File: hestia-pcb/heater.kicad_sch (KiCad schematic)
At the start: 22 parts, among them Q1 FDS8876, SW2 SW_Push_Open, U10 INA826

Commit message: shift template designator/value locations for SRP5030C footprint in library. Update hestia PCB with SRP5030C footprint for L2 on buck regulator. change D7 footprint from SOT23 to smaller SOT-323 as per diode on BOM.
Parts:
- D7: footprint Package_TO_SOT_SMD:SOT-23 -> Package_TO_SOT_SMD:SOT-323_SC-70_Handsoldering
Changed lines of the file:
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@@
       (effects (font (size 1.27 1.27)) (justify left))
     )
-    (property "Footprint" "Package_TO_SOT_SMD:SOT-23" (at 59.055 49.53 0)
+    (property "Footprint" "Package_TO_SOT_SMD:SOT-323_SC-70_Handsoldering" (at 59.055 49.53 0)
       (effects (font (size 1.27 1.27)) (justify left) hide)
     )

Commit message: #28: bump version to 2.1
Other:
- company: (none) -> Mawson Rovers
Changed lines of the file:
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@@
 (kicad_sch (version 20230121) (generator eeschema)
   (paper "A4")
+  (title_block
+    (company "Mawson Rovers")
+  )
   (junction (at 103.505 56.515) (diameter 0) (color 0 0 0 0)
   )

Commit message: added new themal switch footprint to hestia lib. Added 3 wire restraint hole footprints -> 1.2mm, 1.8mm and 1.9mm. Change adc wire restraint holes (H9 to H13) to 1.8mm. Change uC wire restraint holes(H14 & H15) to 1.8mm & moved H14 & H15 designators. Change thermal switch wire restraint holes (H16 & H17) to 1.9mm & also shifted hole coords left 0.2mm & moved H16 & H17 designators. Change thermal switch footprint to new footprint with thruhole pads to 1.2mm dia hole as well as with increased pad distance. Thicken VCC traces to thermal switch - have to revisit to satisfy DRC - probably change multiple traces to signal polygon. Added two GND vias for extra GND stitching off J2. ToDo -Resolve DRC issues. Some padd may need extra signal spurs to pads - just manually adding a trace to the pads may satisfy the DRC requirement
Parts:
- SW2: footprint Connector_PinHeader_2.54mm:PinHeader_1x02_P2.54mm_Vertical -> Hestia:Thermal Switch
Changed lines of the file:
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@@
       (effects (font (size 1.27 1.27)) (justify right))
     )
-    (property "Footprint" "Connector_PinHeader_2.54mm:PinHeader_1x02_P2.54mm_Vertical" (at 124.46 78.74 0)
+    (property "Footprint" "Hestia:Thermal Switch" (at 124.46 78.74 0)
       (effects (font (size 1.27 1.27)) hide)
     )

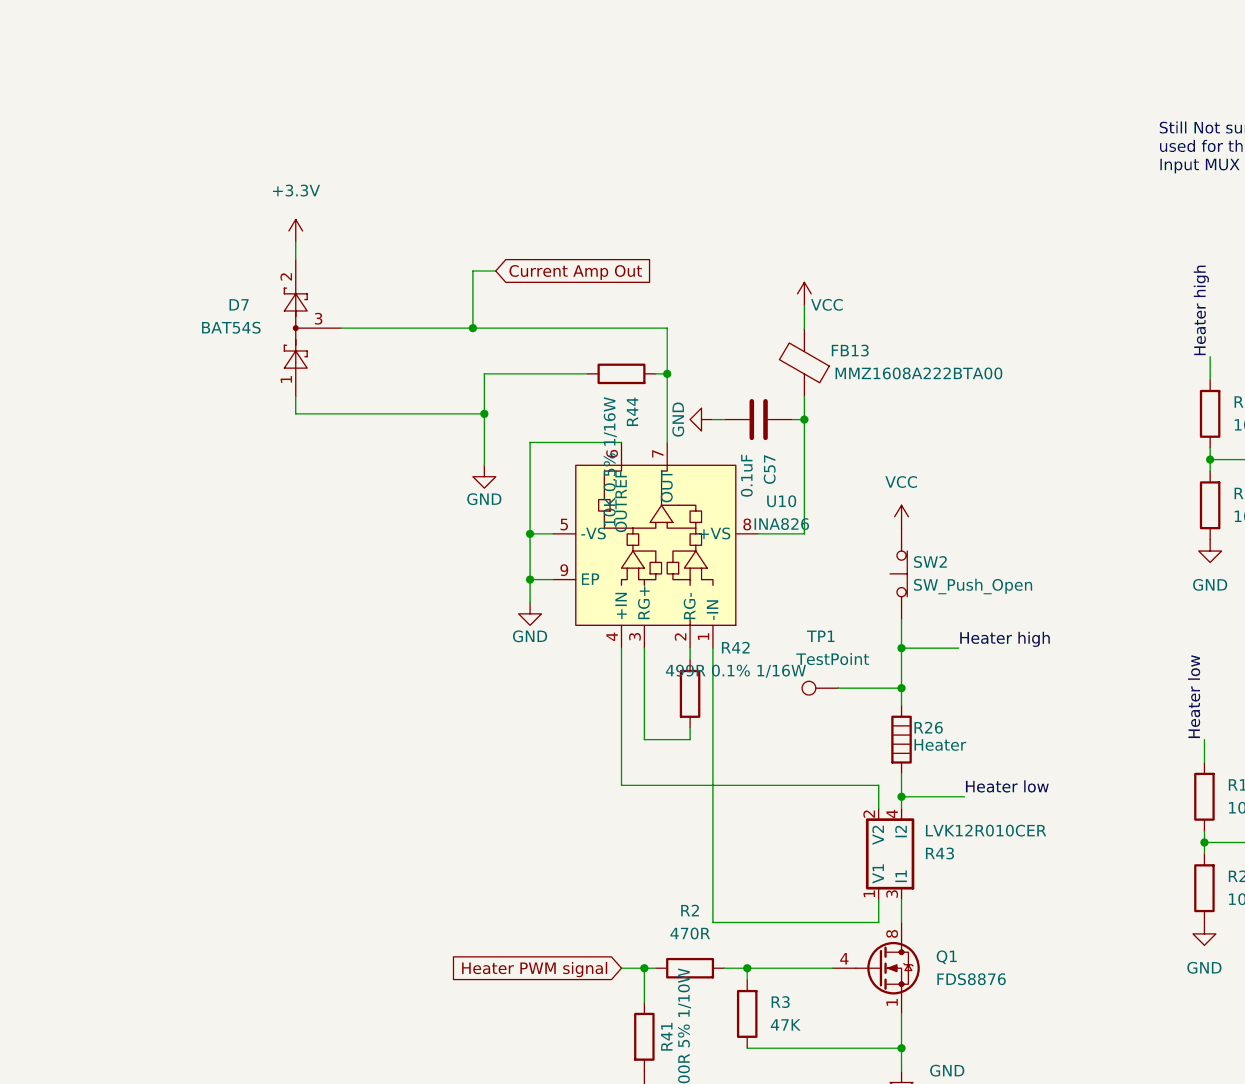
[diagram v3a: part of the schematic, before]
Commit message: #35: add TP7 low side heater test point to schematic
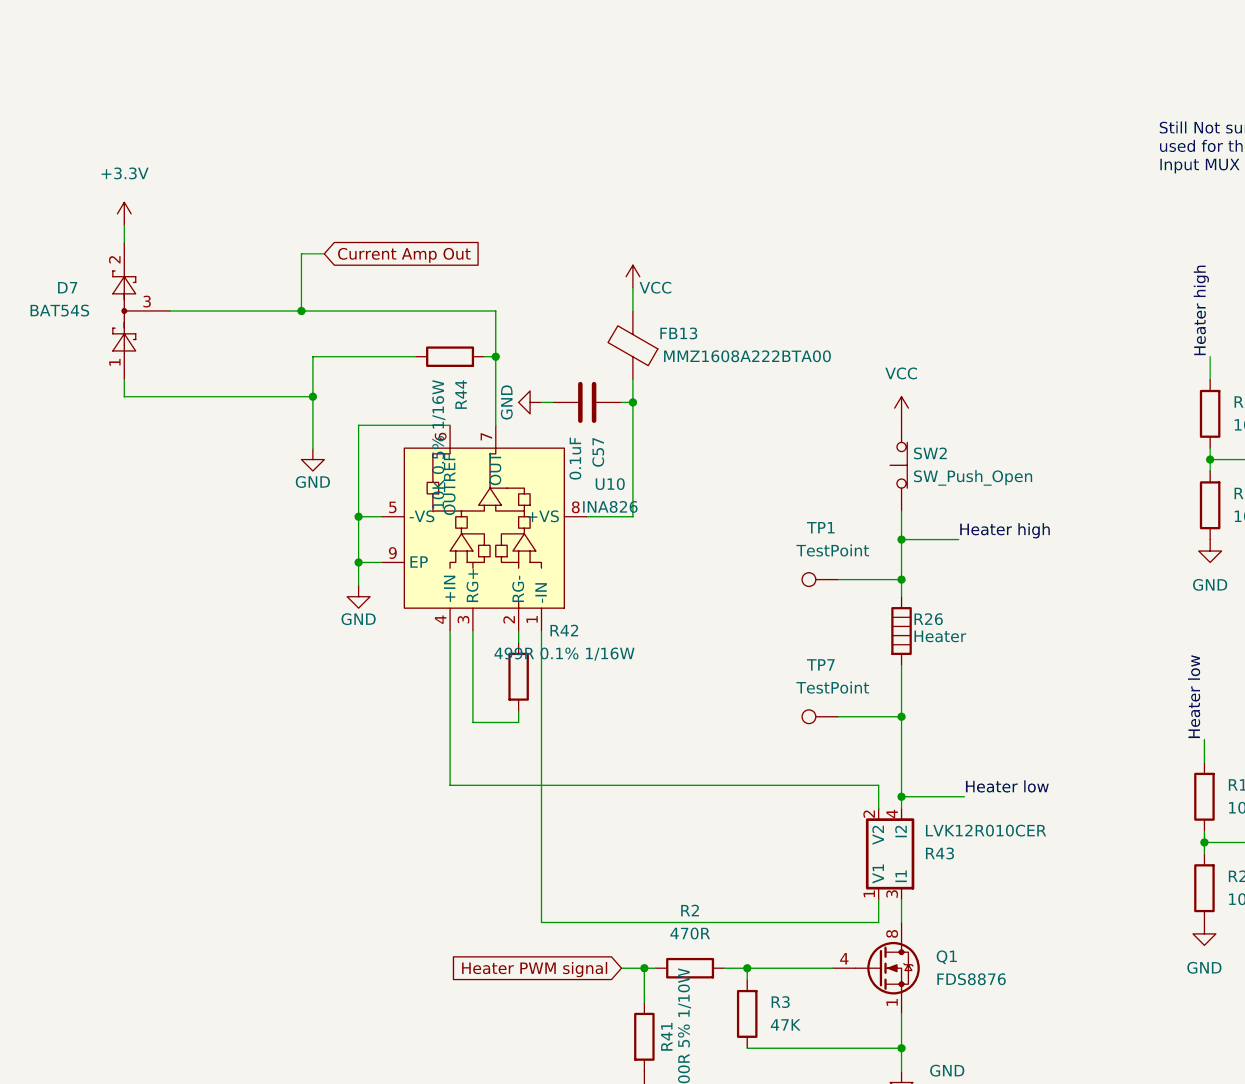
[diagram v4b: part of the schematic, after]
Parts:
- added TP7: TestPoint, TestPoint:TestPoint_Pad_1.0x1.0mm, symbol Connector:TestPoint
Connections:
- net Heater low: now also TP7.1
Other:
- moved on the sheet: C57, D7, FB13, R26, R42, R44, SW2, TP1, U10

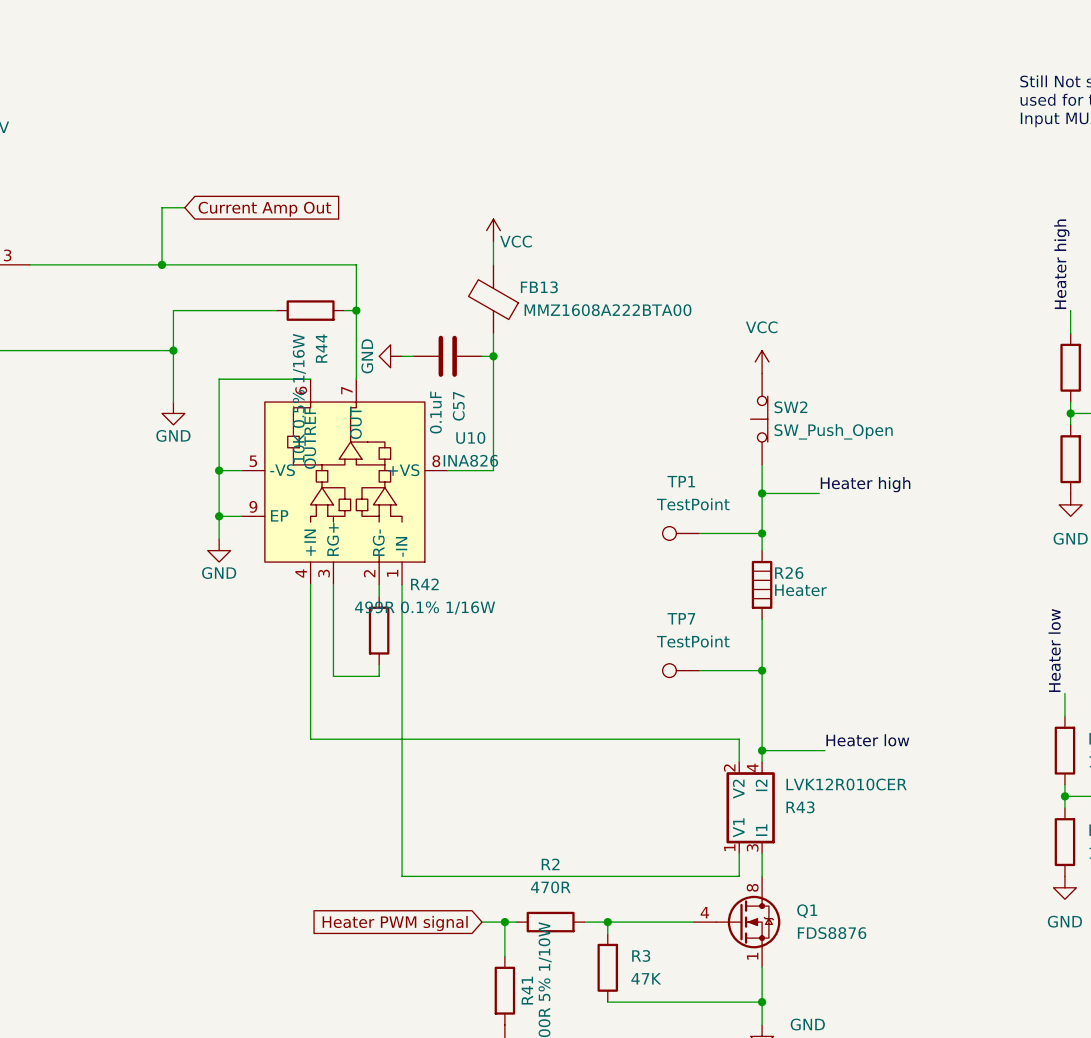
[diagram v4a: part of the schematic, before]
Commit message: reroute current amp out with option resistor to current amp in to directly measure voltage on that side of the current sense resistor. Via added to assist that signal route. add series resistor to current sense line towards uC for current limiting in the case that the low side of the current limiting resistor is experiencing 5V.
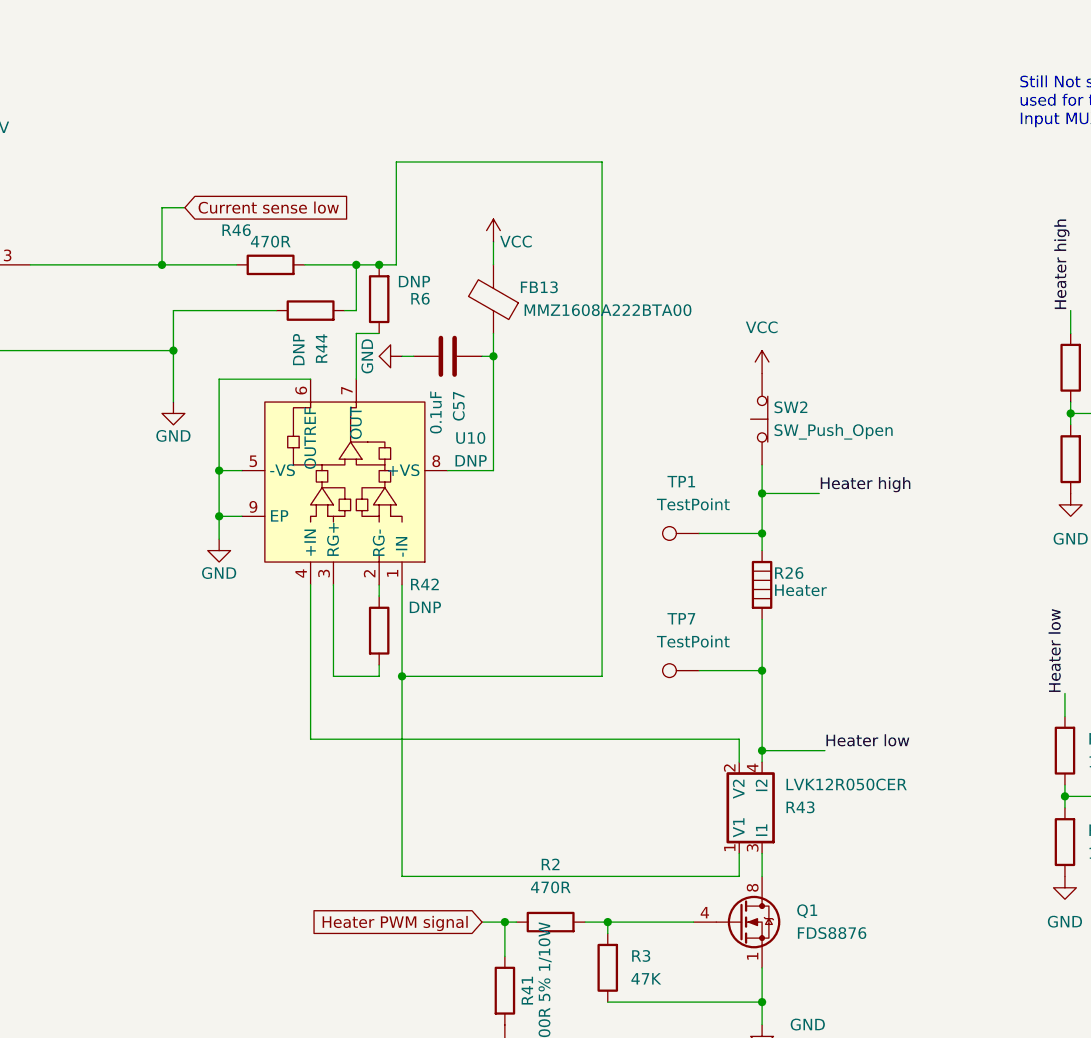
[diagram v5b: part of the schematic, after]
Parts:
- added R46: 470R, Resistor_SMD:R_0603_1608Metric_Pad0.98x0.95mm_HandSolder, symbol Device:R
- added R6: DNP, Resistor_SMD:R_0402_1005Metric_Pad0.72x0.64mm_HandSolder, symbol Device:R
- R42: value 499R 0.1% 1/16W -> DNP
- R43: value LVK12R010CER -> LVK12R050CER; Digikey Part 273-LVK12R010CERCT-ND -> 273-LVK12R050CERCT-ND
- R44: value 10K 0.5% 1/16W -> DNP
- U10: value INA826 -> DNP
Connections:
- net at R43.1 (V1), U10.1 (-IN): now also R44.2, R46.2, R6.2
- removed net Current Amp Out: D7.3, R44.2, U10.7 (OUT)
- new net: R6.1, U10.7 (OUT)
- new net Current sense low: D7.3, R46.1
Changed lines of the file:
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@@
     (company "Mawson Rovers")
   )
-  (junction (at 84.455 54.61) (diameter 0) (color 0 0 0 0)
-  )
   (junction (at 129.54 79.375) (diameter 0) (color 0 0 0 0)
   )
@@
   (junction (at 129.54 94.615) (diameter 0) (color 0 0 0 0)
   )
+  (junction (at 89.535 95.25) (diameter 0) (color 0 0 0 0)
+  )
   (junction (at 64.135 59.055) (diameter 0) (color 0 0 0 0)
   )
+  (junction (at 86.995 49.53) (diameter 0) (color 0 0 0 0)
+  )
   (junction (at 217.805 72.39) (diameter 0) (color 0 0 0 0)
   )
+  (junction (at 84.455 49.53) (diameter 0) (color 0 0 0 0)
+  )
   (junction (at 129.54 131.445) (diameter 0) (color 0 0 0 0)
   )
@@
     (stroke (width 0) (type default))
   )
-  (wire (pts (xy 62.865 49.53) (xy 84.455 49.53))
+  (wire (pts (xy 62.865 49.53) (xy 71.12 49.53))
     (stroke (width 0) (type default))
   )
@@
     (stroke (width 0) (type default))
   )
-  (wire (pts (xy 89.535 85.09) (xy 89.535 117.475))
+  (wire (pts (xy 89.535 85.09) (xy 89.535 95.25))
     (stroke (width 0) (type default))
   )
@@
     (stroke (width 0) (type default))
   )
+  (wire (pts (xy 111.76 95.25) (xy 111.76 38.1))
+    (stroke (width 0) (type default))
+  )
   (wire (pts (xy 129.54 74.93) (xy 135.89 74.93))
     (stroke (width 0) (type default))
@@
     (stroke (width 0) (type default))
   )
-  (wire (pts (xy 84.455 62.23) (xy 84.455 54.61))
-    (stroke (width 0) (type default))
-  )
   (wire (pts (xy 129.54 127.635) (xy 129.54 131.445))
     (stroke (width 0) (type default))
@@
     (stroke (width 0) (type default))
   )
+  (wire (pts (xy 89.535 95.25) (xy 89.535 117.475))
+    (stroke (width 0) (type default))
+  )
   (wire (pts (xy 69.215 72.39) (xy 69.215 77.47))
     (stroke (width 0) (type default))
   )
+  (wire (pts (xy 84.455 57.15) (xy 84.455 62.23))
+    (stroke (width 0) (type default))
+  )
+  (wire (pts (xy 84.455 57.15) (xy 86.995 57.15))
+    (stroke (width 0) (type default))
+  )
   (wire (pts (xy 122.555 94.615) (xy 129.54 94.615))
     (stroke (width 0) (type default))
@@
     (stroke (width 0) (type default))
   )
+  (wire (pts (xy 111.76 38.1) (xy 88.9 38.1))
+    (stroke (width 0) (type default))
+  )
   (wire (pts (xy 129.54 74.93) (xy 129.54 79.375))
     (stroke (width 0) (type default))
@@
     (stroke (width 0) (type default))
   )
+  (wire (pts (xy 89.535 95.25) (xy 111.76 95.25))
+    (stroke (width 0) (type default))
+  )
+  (wire (pts (xy 78.74 49.53) (xy 84.455 49.53))
+    (stroke (width 0) (type default))
+  )
+  (wire (pts (xy 88.9 38.1) (xy 88.9 49.53))
+    (stroke (width 0) (type default))
+  )
   (wire (pts (xy 64.135 59.055) (xy 64.135 64.77))
     (stroke (width 0) (type default))
@@
     (stroke (width 0) (type default))
   )
+  (wire (pts (xy 88.9 49.53) (xy 86.995 49.53))
+    (stroke (width 0) (type default))
+  )
   (wire (pts (xy 129.54 79.375) (xy 129.54 81.28))
     (stroke (width 0) (type default))
@@
   )
   (wire (pts (xy 99.695 57.15) (xy 99.695 59.69))
+    (stroke (width 0) (type default))
+  )
+  (wire (pts (xy 86.995 49.53) (xy 84.455 49.53))
     (stroke (width 0) (type default))
   )
@@
     )
   )
-  (global_label "Current Amp Out" (shape input) (at 65.405 43.18 0) (fields_autoplaced)
+  (global_label "Current sense low" (shape input) (at 65.405 43.18 0) (fields_autoplaced)
     (effects (font (size 1.27 1.27)) (justify left))
-    (property "Intersheetrefs" "${INTERSHEET_REFS}" (at 83.8443 43.1006 0)
+    (property "Intersheetrefs" "${INTERSHEET_REFS}" (at 85.7278 43.18 0)
       (effects (font (size 1.27 1.27)) (justify left) hide)
     )
@@
       (effects (font (size 1.27 1.27)))
     )
-    (property "Value" "INA826" (at 97.155 71.3486 90)
+    (property "Value" "DNP" (at 97.155 71.3486 90)
       (effects (font (size 1.27 1.27)))
     )
@@
     )
   )
+  (symbol (lib_id "Device:R") (at 86.995 53.34 180) (unit 1)
+    (in_bom yes) (on_board yes) (dnp no)
+    (property "Reference" "R6" (at 92.71 53.34 0)
+      (effects (font (size 1.27 1.27)) (justify left))
+    )
+    (property "Value" "DNP" (at 92.71 51.435 0)
+      (effects (font (size 1.27 1.27)) (justify left))
+    )
+    (property "Footprint" "Resistor_SMD:R_0402_1005Metric_Pad0.72x0.64mm_HandSolder" (at 88.773 53.34 90)
+      (effects (font (size 1.27 1.27)) hide)
+    )
+    (property "Datasheet" "~" (at 86.995 53.34 0)
+      (effects (font (size 1.27 1.27)) hide)
+    )
+    (property "Digikey Part" "RMCF0603ZT0R00CT-ND" (at 86.995 53.34 0)
+      (effects (font (size 1.27 1.27)) hide)
+    )
+    (property "Manufacturer" "Stackpole Electronics Inc" (at 86.995 53.34 0)
+      (effects (font (size 1.27 1.27)) hide)
+    )
+    (property "Mfr PN" "RMCF0603ZT0R00" (at 86.995 53.34 0)
+      (effects (font (size 1.27 1.27)) hide)
+    )
+    (property "Type" "SMD" (at 86.995 53.34 0)
+      (effects (font (size 1.27 1.27)) hide)
+    )
+    (pin "1")
+    (pin "2")
+    (instances
+      (project "hestia"
+        (path "/e63e39d7-6ac0-4ffd-8aa3-1841a4541b55"
+          (reference "R6") (unit 1)
+        )
+        (path "/e63e39d7-6ac0-4ffd-8aa3-1841a4541b55/20d49a9a-db00-4709-a347-46ba1cabd595"
+          (reference "R27") (unit 1)
+        )
+      )
+    )
+  )
   (symbol (lib_id "Device:R") (at 106.045 122.555 90) (unit 1)
     (in_bom yes) (on_board yes) (dnp no) (fields_autoplaced)
@@
       (effects (font (size 1.27 1.27)))
     )
-    (property "Value" "499R 0.1% 1/16W" (at 92.075 87.63 0)
+    (property "Value" "DNP" (at 92.075 87.63 0)
       (effects (font (size 1.27 1.27)))
     )
@@
       (effects (font (size 1.27 1.27)) (justify right))
     )
-    (property "Value" "10K 0.5% 1/16W" (at 78.1051 57.15 0)
+    (property "Value" "DNP" (at 78.1051 57.15 0)
       (effects (font (size 1.27 1.27)) (justify right))
     )
@@
       (effects (font (size 1.27 1.27)) (justify right))
     )
-    (property "Value" "LVK12R010CER" (at 132.08 107.315 0)
+    (property "Value" "LVK12R050CER" (at 132.08 107.315 0)
       (effects (font (size 1.27 1.27)) (justify right))
     )
@@
       (effects (font (size 1.27 1.27)) hide)
     )
-    (property "Digikey Part" "273-LVK12R010CERCT-ND" (at 129.54 109.855 0)
+    (property "Digikey Part" "273-LVK12R050CERCT-ND" (at 129.54 109.855 0)
       (effects (font (size 1.27 1.27)) hide)
     )
@@
         )
       )
+    )
+  )
+  (symbol (lib_id "Device:R") (at 74.93 49.53 90) (unit 1)
+    (in_bom yes) (on_board yes) (dnp no)
+    (property "Reference" "R46" (at 71.12 45.72 90)
+      (effects (font (size 1.27 1.27)))
+    )
+    (property "Value" "470R" (at 74.93 46.99 90)
+      (effects (font (size 1.27 1.27)))
+    )
+    (property "Footprint" "Resistor_SMD:R_0603_1608Metric_Pad0.98x0.95mm_HandSolder" (at 74.93 51.308 90)
+      (effects (font (size 1.27 1.27)) hide)
+    )
+    (property "Datasheet" "~" (at 74.93 49.53 0)
+      (effects (font (size 1.27 1.27)) hide)
+    )
+    (property "Digikey Part" "RHM470ADCT-ND" (at 74.93 49.53 90)
+      (effects (font (size 1.27 1.27)) hide)
+    )
+    (property "Manufacturer" "Rohm Semiconductor" (at 74.93 49.53 0)
+      (effects (font (size 1.27 1.27)) hide)
+    )
+    (property "Mfr PN" "ESR03EZPF4700" (at 74.93 49.53 0)
+      (effects (font (size 1.27 1.27)) hide)
+    )
+    (property "Type" "SMD" (at 74.93 49.53 0)
+      (effects (font (size 1.27 1.27)) hide)
+    )
+    (pin "1")
+    (pin "2")
+    (instances
+      (project "hestia"
+        (path "/e63e39d7-6ac0-4ffd-8aa3-1841a4541b55/20d49a9a-db00-4709-a347-46ba1cabd595"
+          (reference "R46") (unit 1)
+        )
+      )
